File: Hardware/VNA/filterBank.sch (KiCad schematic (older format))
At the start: 18 parts, among them U10 74AHC1G04, U11 PE42440, U12 SN74LVC1G139, U13 PE42440

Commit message: first day of layout / routing done
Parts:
- FL1: renamed from FL3; value LFCN-105+ -> LFCN-225+
- FL2: renamed from FL4; value LFCN-225+ -> LFCN-400+
- FL3: renamed from FL5; value LFCN-400+ -> LFCN-1000+
- FL4: renamed from FL6; value LFCN-1000+ -> LFCN-1500+
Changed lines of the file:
@@
 	1    0    0    -1
 $EndComp
-Text Label 4600 2250 2    50   ~ 6
+Text Label 4600 2250 2    50   ~ 10
 SW_1_RF_1
-Text Label 4600 2350 2    50   ~ 6
+Text Label 4600 2350 2    50   ~ 10
 SW_1_RF_2
-Text Label 4600 2450 2    50   ~ 6
+Text Label 4600 2450 2    50   ~ 10
 SW_1_RF_3
-Text Label 4600 2550 2    50   ~ 6
+Text Label 4600 2550 2    50   ~ 10
 SW_1_RF_4
-Text Label 6650 2250 2    50   ~ 6
+Text Label 6650 2250 2    50   ~ 10
 SW_2_RF_3
-Text Label 6650 2950 2    50   ~ 6
+Text Label 6650 2950 2    50   ~ 10
 SW_2_RF_4
 $Comp
@@
 	1    0    0    -1
 $EndComp
-Text Label 3000 6500 2    50   ~ 6
+Text Label 3000 6500 2    50   ~ 10
 SW_1_CTRL_1
 Wire Wire Line
@@
 	1    0    0    -1
 $EndComp
-Text Label 3000 7550 2    50   ~ 6
+Text Label 3000 7550 2    50   ~ 10
 SW_2_CTRL_1
-Text Label 3000 6600 2    50   ~ 6
+Text Label 3000 6600 2    50   ~ 10
 SW_1_CTRL_2
 Wire Wire Line
@@
 Wire Wire Line
 	1200 7650 3000 7650
-Text Label 3000 7650 2    50   ~ 6
+Text Label 3000 7650 2    50   ~ 10
 SW_2_CTRL_2
-Text Notes 750  5950 0    50   ~ 6
+Text Notes 750  5950 0    50   ~ 10
 SW 1
-Text Notes 800  6050 0    50   ~ 6
-1
-Text Notes 800  6150 0    50   ~ 6
+Text Notes 800  6050 0    50   ~ 10
+1
+Text Notes 800  6150 0    50   ~ 10
 2
-Text Notes 800  6250 0    50   ~ 6
+Text Notes 800  6250 0    50   ~ 10
 3
-Text Notes 800  6350 0    50   ~ 6
+Text Notes 800  6350 0    50   ~ 10
 4
-Text Notes 1050 5950 0    50   ~ 6
+Text Notes 1050 5950 0    50   ~ 10
 CTRL 1
-Text Notes 1400 5950 0    50   ~ 6
+Text Notes 1400 5950 0    50   ~ 10
 CTRL 2
 Wire Notes Line
@@
 Wire Notes Line
 	1350 5900 1350 6350
-Text Notes 1500 6050 0    50   ~ 6
-0
-Text Notes 1500 6250 0    50   ~ 6
-0
-Text Notes 1500 6150 0    50   ~ 6
-1
-Text Notes 1500 6350 0    50   ~ 6
-1
-Text Notes 1900 5950 0    50   ~ 6
+Text Notes 1500 6050 0    50   ~ 10
+0
+Text Notes 1500 6250 0    50   ~ 10
+0
+Text Notes 1500 6150 0    50   ~ 10
+1
+Text Notes 1500 6350 0    50   ~ 10
+1
+Text Notes 1900 5950 0    50   ~ 10
 SW 2
-Text Notes 1950 6250 0    50   ~ 6
-1
-Text Notes 1950 6350 0    50   ~ 6
+Text Notes 1950 6250 0    50   ~ 10
+1
+Text Notes 1950 6350 0    50   ~ 10
 2
-Text Notes 1950 6050 0    50   ~ 6
+Text Notes 1950 6050 0    50   ~ 10
 3
-Text Notes 1950 6150 0    50   ~ 6
+Text Notes 1950 6150 0    50   ~ 10
 4
-Text Notes 2200 5950 0    50   ~ 6
+Text Notes 2200 5950 0    50   ~ 10
 CTRL 1
-Text Notes 2550 5950 0    50   ~ 6
+Text Notes 2550 5950 0    50   ~ 10
 CTRL 2
 Wire Notes Line
@@
 Wire Notes Line
 	2500 5900 2500 6350
-Text Notes 2650 6050 0    50   ~ 6
-0
-Text Notes 2650 6250 0    50   ~ 6
-0
-Text Notes 2650 6150 0    50   ~ 6
-1
-Text Notes 2650 6350 0    50   ~ 6
+Text Notes 2650 6050 0    50   ~ 10
+0
+Text Notes 2650 6250 0    50   ~ 10
+0
+Text Notes 2650 6150 0    50   ~ 10
+1
+Text Notes 2650 6350 0    50   ~ 10
 1
 Wire Notes Line
@@
 Wire Notes Line
 	700  5950 1700 5950
-Text Notes 1150 6050 0    50   ~ 6
-0
-Text Notes 1150 6150 0    50   ~ 6
-0
-Text Notes 1150 6250 0    50   ~ 6
-1
-Text Notes 1150 6350 0    50   ~ 6
-1
-Text Notes 2300 6050 0    50   ~ 6
-1
-Text Notes 2300 6150 0    50   ~ 6
-1
-Text Notes 2300 6250 0    50   ~ 6
-0
-Text Notes 2300 6350 0    50   ~ 6
-0
-Text Notes 950  5400 0    100  ~ 6
+Text Notes 1150 6050 0    50   ~ 10
+0
+Text Notes 1150 6150 0    50   ~ 10
+0
+Text Notes 1150 6250 0    50   ~ 10
+1
+Text Notes 1150 6350 0    50   ~ 10
+1
+Text Notes 2300 6050 0    50   ~ 10
+1
+Text Notes 2300 6150 0    50   ~ 10
+1
+Text Notes 2300 6250 0    50   ~ 10
+0
+Text Notes 2300 6350 0    50   ~ 10
+0
+Text Notes 950  5400 0    100  ~ 20
 Switch Configuration\n
-Text Notes 850  5750 0    50   ~ 6
+Text Notes 850  5750 0    50   ~ 10
 74AHC1G04 is a not gate, used to allow the below \ntruth tables to be correct with only two control\nlines following the values in the first table
 Wire Wire Line
@@
 Wire Wire Line
 	1400 6500 3000 6500
-Text Label 6700 3650 2    50   ~ 6
+Text Label 6700 3650 2    50   ~ 10
 SW_2_RF_1
-Text Label 6700 4400 2    50   ~ 6
+Text Label 6700 4400 2    50   ~ 10
 SW_2_RF_2
 $Comp
-L VNA_Symbols:Filter_LFCN FL3
+L VNA_Symbols:Filter_LFCN FL1
 U 1 1 5C37DE93
 P 5700 2350
-F 0 "FL3" H 5725 2675 50  0000 C CNN
-F 1 "LFCN-105+" H 5725 2584 50  0000 C CNN
+F 0 "FL1" H 5725 2675 50  0000 C CNN
+F 1 "LFCN-225+" H 5725 2584 50  0000 C CNN
 F 2 "VNA_Footprints:FV1206" H 5700 2500 50  0001 C CNN
 F 3 "" H 5700 2500 50  0001 C CNN
@@
 $EndComp
 $Comp
-L VNA_Symbols:Filter_LFCN FL4
+L VNA_Symbols:Filter_LFCN FL2
 U 1 1 5C3813C7
 P 5700 3050
-F 0 "FL4" H 5725 3375 50  0000 C CNN
-F 1 "LFCN-225+" H 5725 3284 50  0000 C CNN
+F 0 "FL2" H 5725 3375 50  0000 C CNN
+F 1 "LFCN-400+" H 5725 3284 50  0000 C CNN
 F 2 "VNA_Footprints:FV1206" H 5700 3200 50  0001 C CNN
 F 3 "" H 5700 3200 50  0001 C CNN
@@
 $EndComp
 $Comp
-L VNA_Symbols:Filter_LFCN FL5
+L VNA_Symbols:Filter_LFCN FL3
 U 1 1 5C394D09
 P 5700 3750
-F 0 "FL5" H 5725 4075 50  0000 C CNN
-F 1 "LFCN-400+" H 5725 3984 50  0000 C CNN
+F 0 "FL3" H 5725 4075 50  0000 C CNN
+F 1 "LFCN-1000+" H 5725 3984 50  0000 C CNN
 F 2 "VNA_Footprints:FV1206" H 5700 3900 50  0001 C CNN
 F 3 "" H 5700 3900 50  0001 C CNN
@@
 $EndComp
 $Comp
-L VNA_Symbols:Filter_LFCN FL6
+L VNA_Symbols:Filter_LFCN FL4
 U 1 1 5C3A1E64
 P 5700 4500
-F 0 "FL6" H 5725 4825 50  0000 C CNN
-F 1 "LFCN-1000+" H 5725 4734 50  0000 C CNN
+F 0 "FL4" H 5725 4825 50  0000 C CNN
+F 1 "LFCN-1500+" H 5725 4734 50  0000 C CNN
 F 2 "VNA_Footprints:FV1206" H 5700 4650 50  0001 C CNN
 F 3 "" H 5700 4650 50  0001 C CNN
@@
 Wire Wire Line
 	3250 1800 3250 1950
-Text Notes 5300 1750 0    100  ~ 6
+Text Notes 5300 1750 0    100  ~ 20
 Filter Bank
-Text Notes 3050 1350 0    100  ~ 6
+Text Notes 3050 1350 0    100  ~ 20
 Switch 1
-Text Notes 8150 1400 0    100  ~ 6
+Text Notes 8150 1400 0    100  ~ 20
 Switch 2
 Connection ~ 1200 6600
@@
 Wire Wire Line
 	1400 6500 850  6500
-Text HLabel 2500 2250 0    50   Input ~ 6
+Text HLabel 2500 2250 0    50   Input ~ 10
 RF_IN
-Text HLabel 9200 2300 2    50   Input ~ 6
+Text HLabel 9200 2300 2    50   Input ~ 10
 RF_OUT
-Text HLabel 850  6500 0    50   Input ~ 6
+Text HLabel 850  6500 0    50   Input ~ 10
 CTRL1
-Text HLabel 850  6600 0    50   Input ~ 6
+Text HLabel 850  6600 0    50   Input ~ 10
 CTRL2
 Wire Wire Line
@@
 Wire Wire Line
 	2600 2450 2050 2450
-Text Label 2050 2550 0    50   ~ 6
+Text Label 2050 2550 0    50   ~ 10
 SW_1_CTRL_2
-Text Label 2050 2450 0    50   ~ 6
+Text Label 2050 2450 0    50   ~ 10
 SW_1_CTRL_1
 $Comp
@@
 Wire Wire Line
 	9100 2500 9650 2500
-Text Label 9650 2600 2    50   ~ 6
+Text Label 9650 2600 2    50   ~ 10
 SW_2_CTRL_2
-Text Label 9650 2500 2    50   ~ 6
+Text Label 9650 2500 2    50   ~ 10
 SW_2_CTRL_1
 Wire Wire Line
@@
 Wire Wire Line
 	6150 4400 7200 4400
-Text HLabel 3250 1650 1    50   Input ~ 6
+Text HLabel 3250 1650 1    50   Input ~ 10
 3V3A
-Text HLabel 8450 1700 1    50   Input ~ 6
+Text HLabel 8450 1700 1    50   Input ~ 10
 3V3A
-Text HLabel 2300 6850 2    50   Input ~ 6
+Text HLabel 2300 6850 2    50   Input ~ 10
 3V3A
 Wire Wire Line
@@
 	1    0    0    -1
 $EndComp
-Text HLabel 4200 6500 1    50   Input ~ 6
+Text HLabel 4200 6500 1    50   Input ~ 10
 3V3
 Wire Wire Line
 	4200 6500 4200 6700
-Text HLabel 4250 6850 0    50   Input ~ 6
+Text HLabel 4250 6850 0    50   Input ~ 10
 CTRL1
-Text HLabel 4250 6950 0    50   Input ~ 6
+Text HLabel 4250 6950 0    50   Input ~ 10
 CTRL2
 Wire Wire Line
@@
 Wire Wire Line
 	6200 7050 6200 7250
-Text HLabel 6200 6500 1    50   Input ~ 6
+Text HLabel 6200 6500 1    50   Input ~ 10
 3V3
 Wire Wire Line
@@
 	0    -1   -1   0
 $EndComp
-Text Notes 5350 6650 0    50   ~ 6
+Text Notes 5350 6650 0    50   ~ 10
 F1
-Text Notes 5350 6850 0    50   ~ 6
+Text Notes 5350 6850 0    50   ~ 10
 F2
-Text Notes 5350 7050 0    50   ~ 6
+Text Notes 5350 7050 0    50   ~ 10
 F3
-Text Notes 5350 7250 0    50   ~ 6
+Text Notes 5350 7250 0    50   ~ 10
 F4
-Text Notes 4550 6300 0    100  ~ 6
+Text Notes 4550 6300 0    100  ~ 20
 LED Filter Indicator
 $EndSCHEMATC

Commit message: Gerbers generated, ready for fab
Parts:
- U12: footprint VNA_Footprints:VSSOP-8_2.9x3.15mm_P0.65 -> Package_SO:VSSOP-8_2.3x2mm_P0.5mm
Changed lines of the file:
@@
 F 0 "U12" H 4600 7325 50  0000 C CNN
 F 1 "SN74LVC1G139" H 4600 7234 50  0000 C CNN
-F 2 "VNA_Footprints:VSSOP-8_2.9x3.15mm_P0.65" H 4700 7150 100 0001 C CNN
+F 2 "Package_SO:VSSOP-8_2.3x2mm_P0.5mm" H 4700 7150 100 0001 C CNN
 F 3 "" H 4700 7150 100 0001 C CNN
 	1    4600 6900

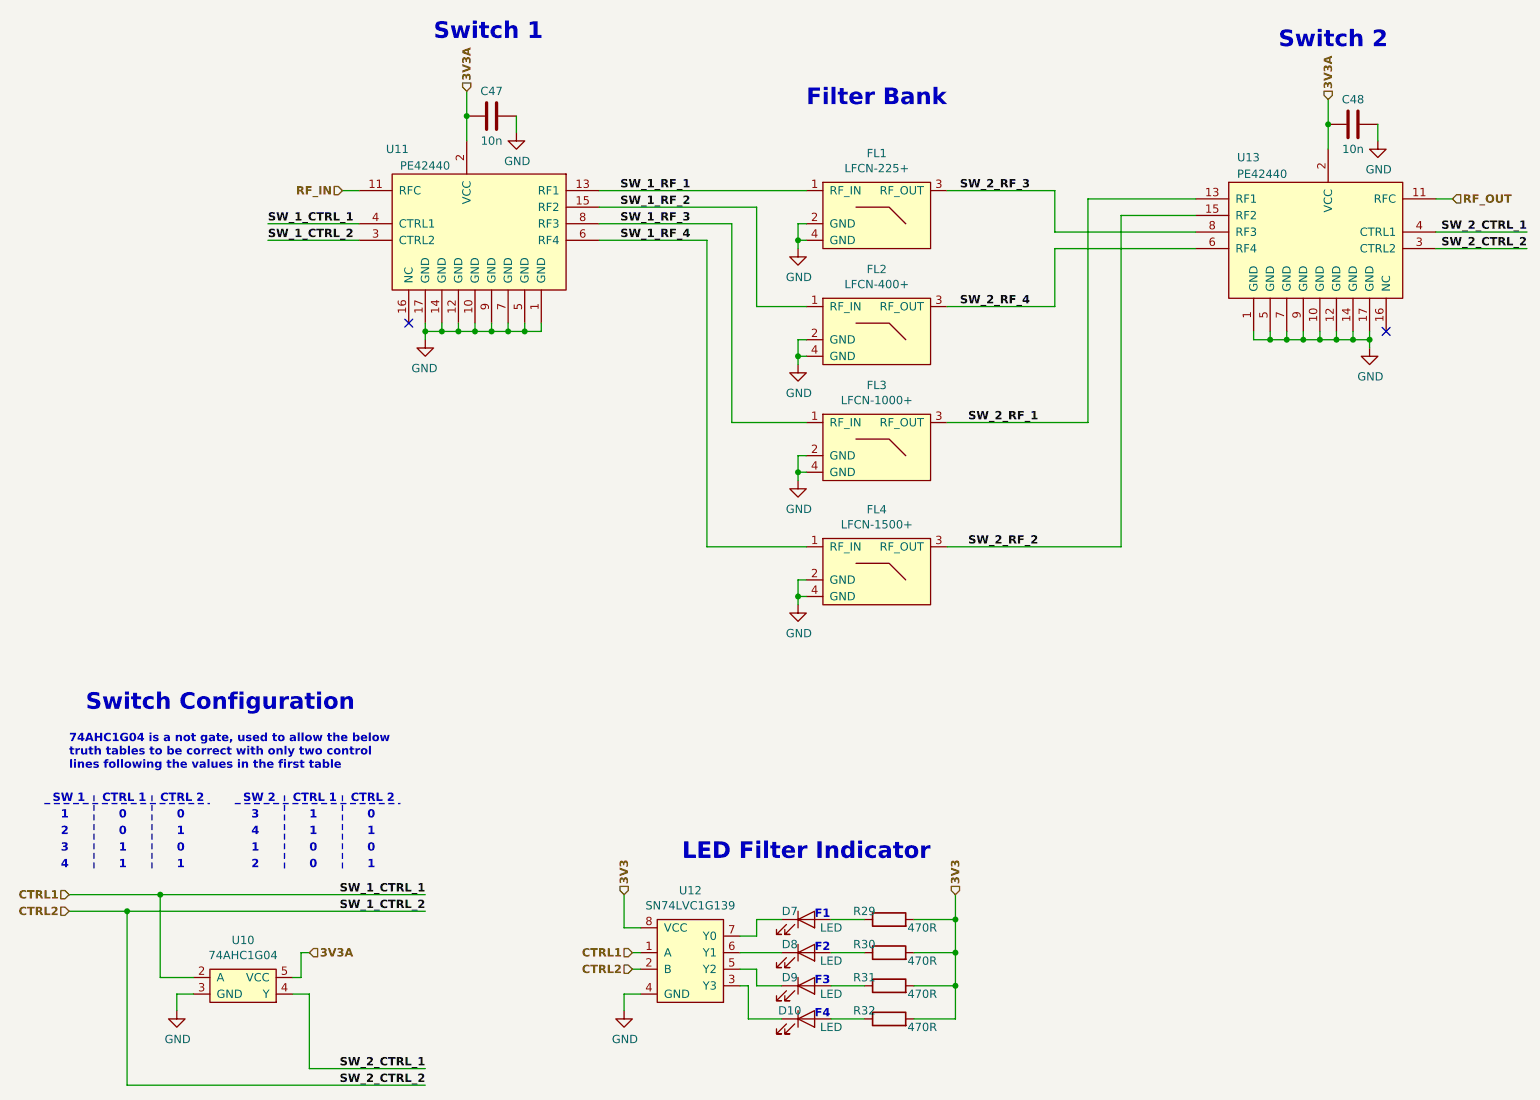
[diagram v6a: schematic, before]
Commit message: fix KiCad 5.1.0 bold after plot issue on schematics
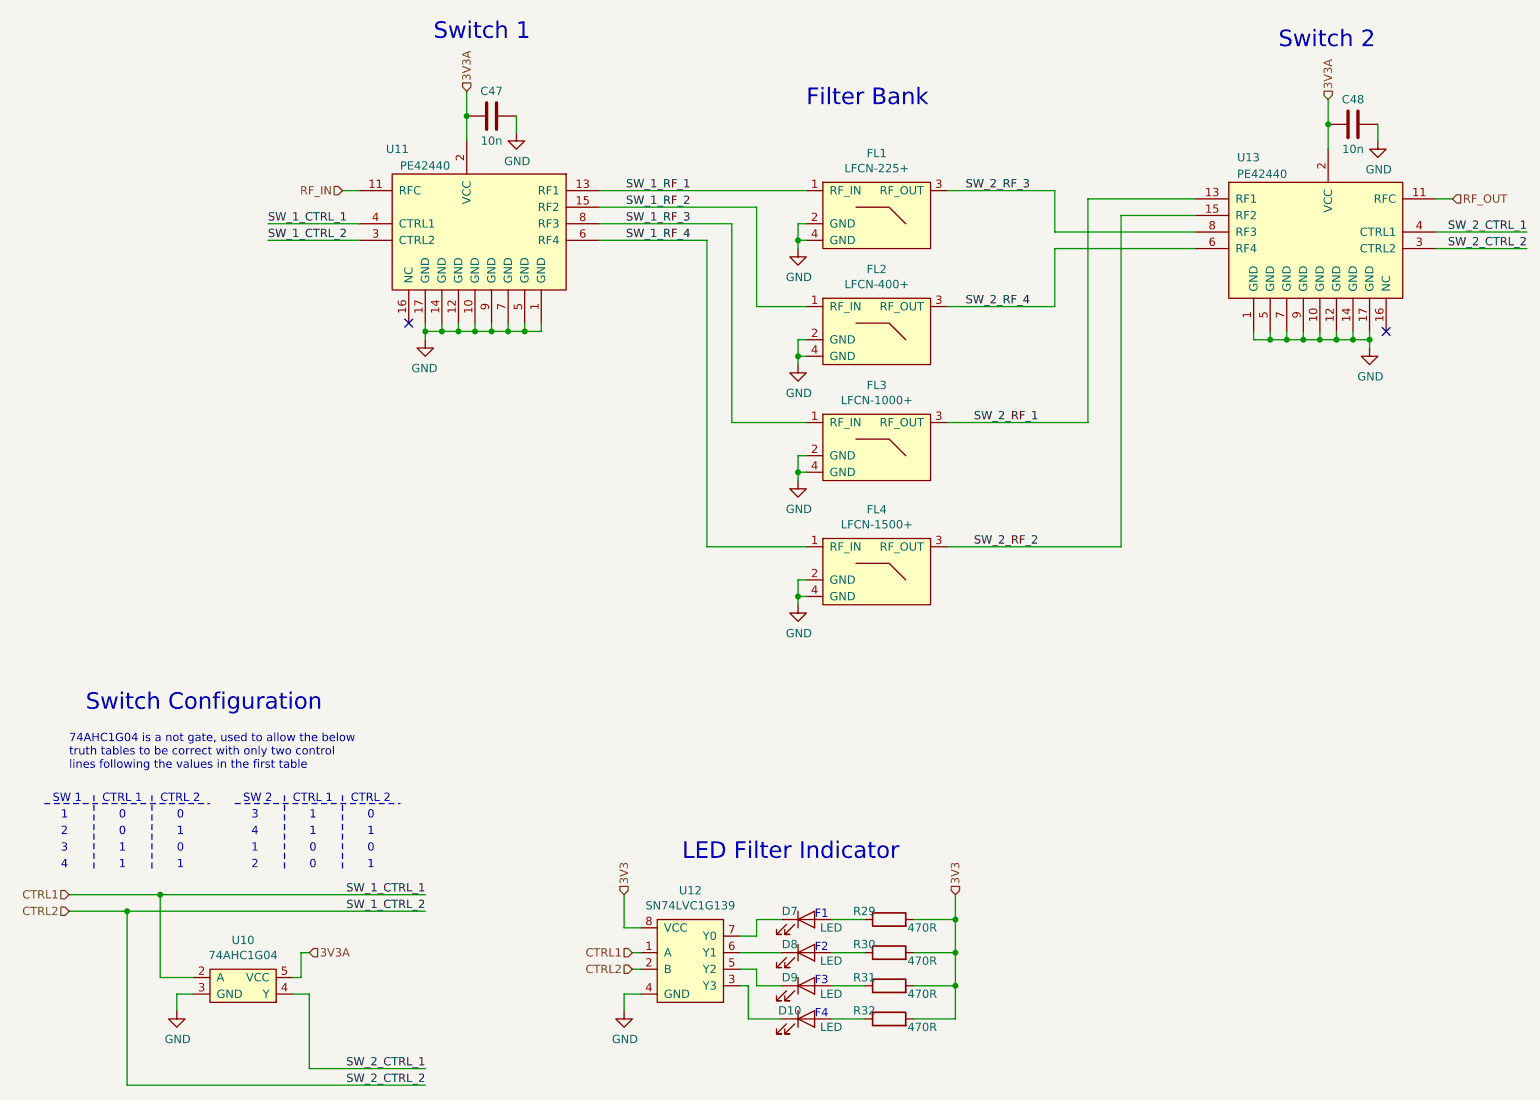
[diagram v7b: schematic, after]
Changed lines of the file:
@@
 	1    0    0    -1
 $EndComp
-Text Label 4600 2250 2    50   ~ 10
+Text Label 4600 2250 2    50   ~ 0
 SW_1_RF_1
-Text Label 4600 2350 2    50   ~ 10
+Text Label 4600 2350 2    50   ~ 0
 SW_1_RF_2
-Text Label 4600 2450 2    50   ~ 10
+Text Label 4600 2450 2    50   ~ 0
 SW_1_RF_3
-Text Label 4600 2550 2    50   ~ 10
+Text Label 4600 2550 2    50   ~ 0
 SW_1_RF_4
-Text Label 6650 2250 2    50   ~ 10
+Text Label 6650 2250 2    50   ~ 0
 SW_2_RF_3
-Text Label 6650 2950 2    50   ~ 10
+Text Label 6650 2950 2    50   ~ 0
 SW_2_RF_4
 $Comp
@@
 	1    0    0    -1
 $EndComp
-Text Label 3000 6500 2    50   ~ 10
+Text Label 3000 6500 2    50   ~ 0
 SW_1_CTRL_1
 Wire Wire Line
@@
 	1    0    0    -1
 $EndComp
-Text Label 3000 7550 2    50   ~ 10
+Text Label 3000 7550 2    50   ~ 0
 SW_2_CTRL_1
-Text Label 3000 6600 2    50   ~ 10
+Text Label 3000 6600 2    50   ~ 0
 SW_1_CTRL_2
 Wire Wire Line
@@
 Wire Wire Line
 	1200 7650 3000 7650
-Text Label 3000 7650 2    50   ~ 10
+Text Label 3000 7650 2    50   ~ 0
 SW_2_CTRL_2
-Text Notes 750  5950 0    50   ~ 10
+Text Notes 750  5950 0    50   ~ 0
 SW 1
-Text Notes 800  6050 0    50   ~ 10
-1
-Text Notes 800  6150 0    50   ~ 10
+Text Notes 800  6050 0    50   ~ 0
+1
+Text Notes 800  6150 0    50   ~ 0
 2
-Text Notes 800  6250 0    50   ~ 10
+Text Notes 800  6250 0    50   ~ 0
 3
-Text Notes 800  6350 0    50   ~ 10
+Text Notes 800  6350 0    50   ~ 0
 4
-Text Notes 1050 5950 0    50   ~ 10
+Text Notes 1050 5950 0    50   ~ 0
 CTRL 1
-Text Notes 1400 5950 0    50   ~ 10
+Text Notes 1400 5950 0    50   ~ 0
 CTRL 2
 Wire Notes Line
@@
 Wire Notes Line
 	1350 5900 1350 6350
-Text Notes 1500 6050 0    50   ~ 10
-0
-Text Notes 1500 6250 0    50   ~ 10
-0
-Text Notes 1500 6150 0    50   ~ 10
-1
-Text Notes 1500 6350 0    50   ~ 10
-1
-Text Notes 1900 5950 0    50   ~ 10
+Text Notes 1500 6050 0    50   ~ 0
+0
+Text Notes 1500 6250 0    50   ~ 0
+0
+Text Notes 1500 6150 0    50   ~ 0
+1
+Text Notes 1500 6350 0    50   ~ 0
+1
+Text Notes 1900 5950 0    50   ~ 0
 SW 2
-Text Notes 1950 6250 0    50   ~ 10
-1
-Text Notes 1950 6350 0    50   ~ 10
+Text Notes 1950 6250 0    50   ~ 0
+1
+Text Notes 1950 6350 0    50   ~ 0
 2
-Text Notes 1950 6050 0    50   ~ 10
+Text Notes 1950 6050 0    50   ~ 0
 3
-Text Notes 1950 6150 0    50   ~ 10
+Text Notes 1950 6150 0    50   ~ 0
 4
-Text Notes 2200 5950 0    50   ~ 10
+Text Notes 2200 5950 0    50   ~ 0
 CTRL 1
-Text Notes 2550 5950 0    50   ~ 10
+Text Notes 2550 5950 0    50   ~ 0
 CTRL 2
 Wire Notes Line
@@
 Wire Notes Line
 	2500 5900 2500 6350
-Text Notes 2650 6050 0    50   ~ 10
-0
-Text Notes 2650 6250 0    50   ~ 10
-0
-Text Notes 2650 6150 0    50   ~ 10
-1
-Text Notes 2650 6350 0    50   ~ 10
+Text Notes 2650 6050 0    50   ~ 0
+0
+Text Notes 2650 6250 0    50   ~ 0
+0
+Text Notes 2650 6150 0    50   ~ 0
+1
+Text Notes 2650 6350 0    50   ~ 0
 1
 Wire Notes Line
@@
 Wire Notes Line
 	700  5950 1700 5950
-Text Notes 1150 6050 0    50   ~ 10
-0
-Text Notes 1150 6150 0    50   ~ 10
-0
-Text Notes 1150 6250 0    50   ~ 10
-1
-Text Notes 1150 6350 0    50   ~ 10
-1
-Text Notes 2300 6050 0    50   ~ 10
-1
-Text Notes 2300 6150 0    50   ~ 10
-1
-Text Notes 2300 6250 0    50   ~ 10
-0
-Text Notes 2300 6350 0    50   ~ 10
-0
-Text Notes 950  5400 0    100  ~ 20
+Text Notes 1150 6050 0    50   ~ 0
+0
+Text Notes 1150 6150 0    50   ~ 0
+0
+Text Notes 1150 6250 0    50   ~ 0
+1
+Text Notes 1150 6350 0    50   ~ 0
+1
+Text Notes 2300 6050 0    50   ~ 0
+1
+Text Notes 2300 6150 0    50   ~ 0
+1
+Text Notes 2300 6250 0    50   ~ 0
+0
+Text Notes 2300 6350 0    50   ~ 0
+0
+Text Notes 950  5400 0    100  ~ 0
 Switch Configuration\n
-Text Notes 850  5750 0    50   ~ 10
+Text Notes 850  5750 0    50   ~ 0
 74AHC1G04 is a not gate, used to allow the below \ntruth tables to be correct with only two control\nlines following the values in the first table
 Wire Wire Line
@@
 Wire Wire Line
 	1400 6500 3000 6500
-Text Label 6700 3650 2    50   ~ 10
+Text Label 6700 3650 2    50   ~ 0
 SW_2_RF_1
-Text Label 6700 4400 2    50   ~ 10
+Text Label 6700 4400 2    50   ~ 0
 SW_2_RF_2
 $Comp
@@
 Wire Wire Line
 	3250 1800 3250 1950
-Text Notes 5300 1750 0    100  ~ 20
+Text Notes 5300 1750 0    100  ~ 0
 Filter Bank
-Text Notes 3050 1350 0    100  ~ 20
+Text Notes 3050 1350 0    100  ~ 0
 Switch 1
-Text Notes 8150 1400 0    100  ~ 20
+Text Notes 8150 1400 0    100  ~ 0
 Switch 2
 Connection ~ 1200 6600
@@
 Wire Wire Line
 	1400 6500 850  6500
-Text HLabel 2500 2250 0    50   Input ~ 10
+Text HLabel 2500 2250 0    50   Input ~ 0
 RF_IN
-Text HLabel 9200 2300 2    50   Input ~ 10
+Text HLabel 9200 2300 2    50   Input ~ 0
 RF_OUT
-Text HLabel 850  6500 0    50   Input ~ 10
+Text HLabel 850  6500 0    50   Input ~ 0
 CTRL1
-Text HLabel 850  6600 0    50   Input ~ 10
+Text HLabel 850  6600 0    50   Input ~ 0
 CTRL2
 Wire Wire Line
@@
 Wire Wire Line
 	2600 2450 2050 2450
-Text Label 2050 2550 0    50   ~ 10
+Text Label 2050 2550 0    50   ~ 0
 SW_1_CTRL_2
-Text Label 2050 2450 0    50   ~ 10
+Text Label 2050 2450 0    50   ~ 0
 SW_1_CTRL_1
 $Comp
@@
 Wire Wire Line
 	9100 2500 9650 2500
-Text Label 9650 2600 2    50   ~ 10
+Text Label 9650 2600 2    50   ~ 0
 SW_2_CTRL_2
-Text Label 9650 2500 2    50   ~ 10
+Text Label 9650 2500 2    50   ~ 0
 SW_2_CTRL_1
 Wire Wire Line
@@
 Wire Wire Line
 	6150 4400 7200 4400
-Text HLabel 3250 1650 1    50   Input ~ 10
+Text HLabel 3250 1650 1    50   Input ~ 0
 3V3A
-Text HLabel 8450 1700 1    50   Input ~ 10
+Text HLabel 8450 1700 1    50   Input ~ 0
 3V3A
-Text HLabel 2300 6850 2    50   Input ~ 10
+Text HLabel 2300 6850 2    50   Input ~ 0
 3V3A
 Wire Wire Line
@@
 	1    0    0    -1
 $EndComp
-Text HLabel 4200 6500 1    50   Input ~ 10
+Text HLabel 4200 6500 1    50   Input ~ 0
 3V3
 Wire Wire Line
 	4200 6500 4200 6700
-Text HLabel 4250 6850 0    50   Input ~ 10
+Text HLabel 4250 6850 0    50   Input ~ 0
 CTRL1
-Text HLabel 4250 6950 0    50   Input ~ 10
+Text HLabel 4250 6950 0    50   Input ~ 0
 CTRL2
 Wire Wire Line
@@
 Wire Wire Line
 	6200 7050 6200 7250
-Text HLabel 6200 6500 1    50   Input ~ 10
+Text HLabel 6200 6500 1    50   Input ~ 0
 3V3
 Wire Wire Line
@@
 	0    -1   -1   0
 $EndComp
-Text Notes 5350 6650 0    50   ~ 10
+Text Notes 5350 6650 0    50   ~ 0
 F1
-Text Notes 5350 6850 0    50   ~ 10
+Text Notes 5350 6850 0    50   ~ 0
 F2
-Text Notes 5350 7050 0    50   ~ 10
+Text Notes 5350 7050 0    50   ~ 0
 F3
-Text Notes 5350 7250 0    50   ~ 10
+Text Notes 5350 7250 0    50   ~ 0
 F4
-Text Notes 4550 6300 0    100  ~ 20
+Text Notes 4550 6300 0    100  ~ 0
 LED Filter Indicator
 $EndSCHEMATC
